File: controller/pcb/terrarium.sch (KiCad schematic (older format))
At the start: 65 parts, among them K1 G3MB-202P, K2 G3MB-202P, K3 G3MB-202P, Q1 S8050, Q2 S8050, Q3 S8050, SW1 RST, U1 ESP32-WROOM-32, U2 DS3231M, U5 TCA9548APWR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

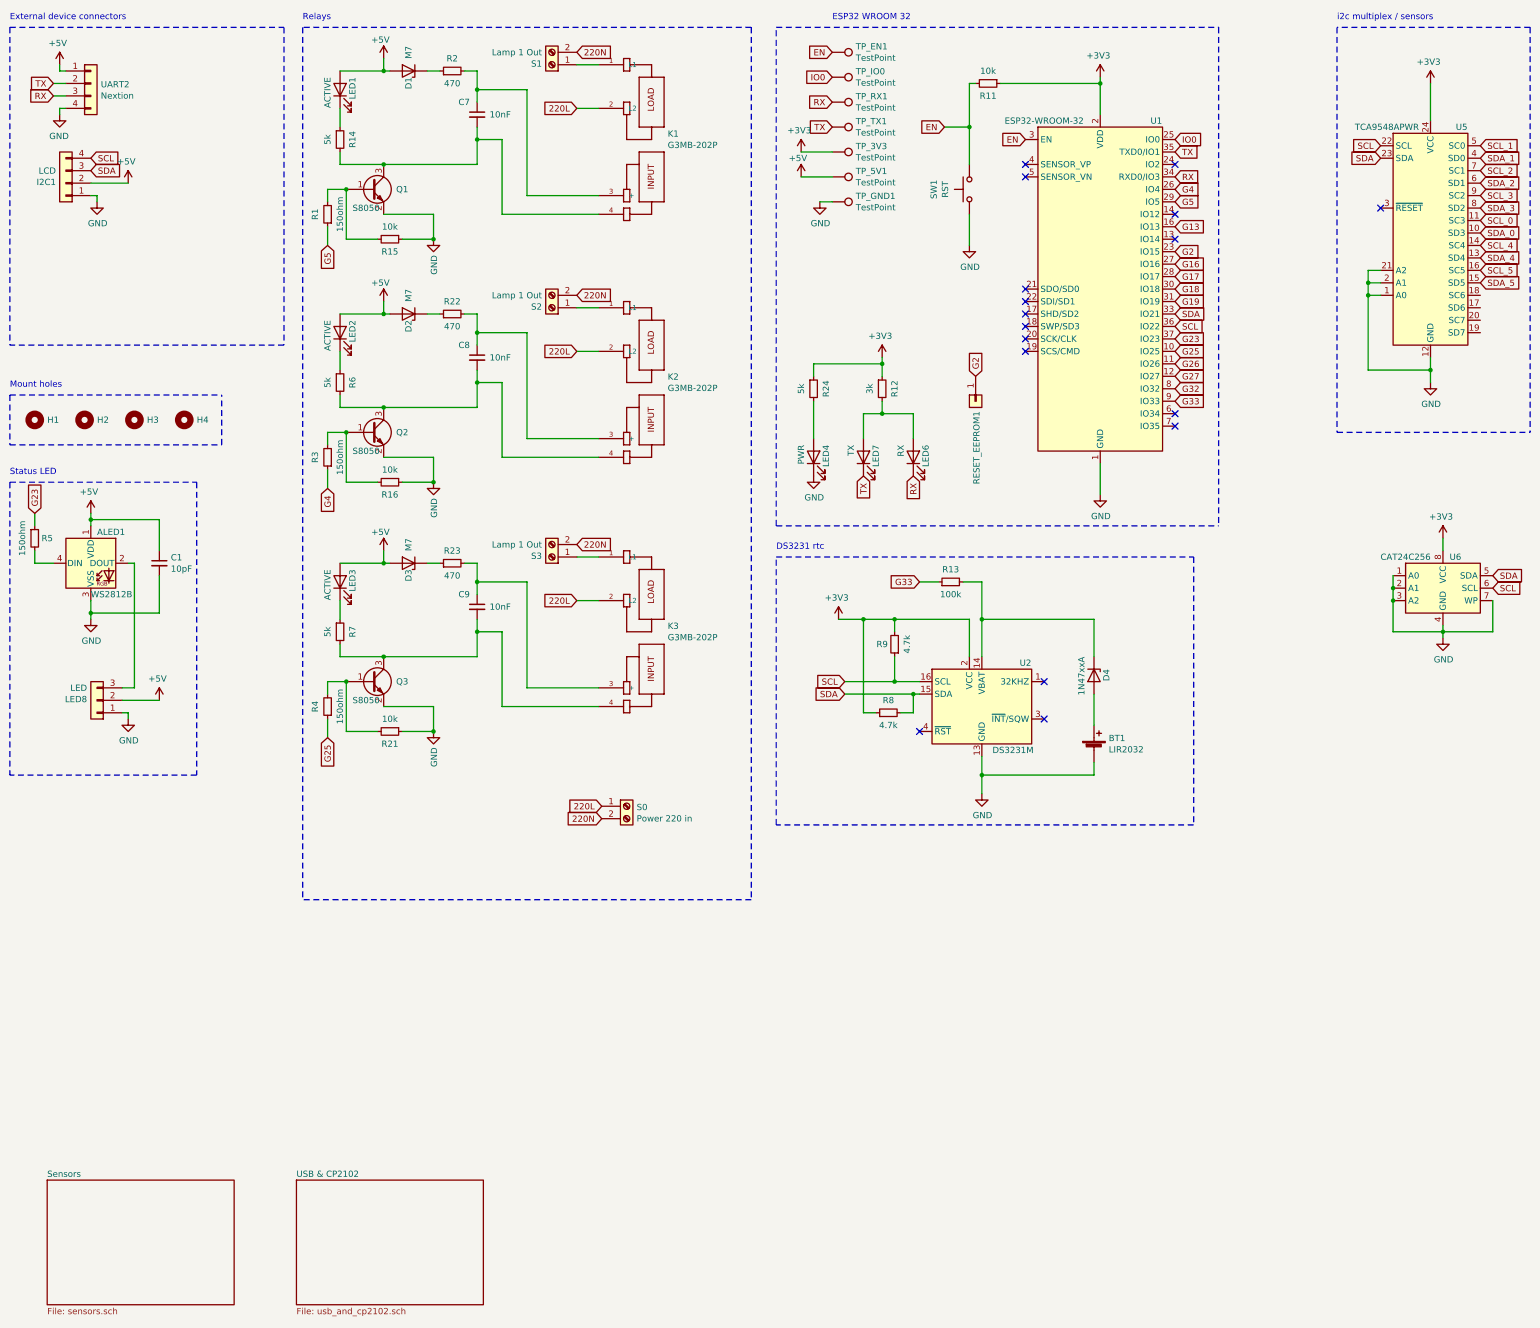
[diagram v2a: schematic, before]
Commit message: improved silk screen, tracing
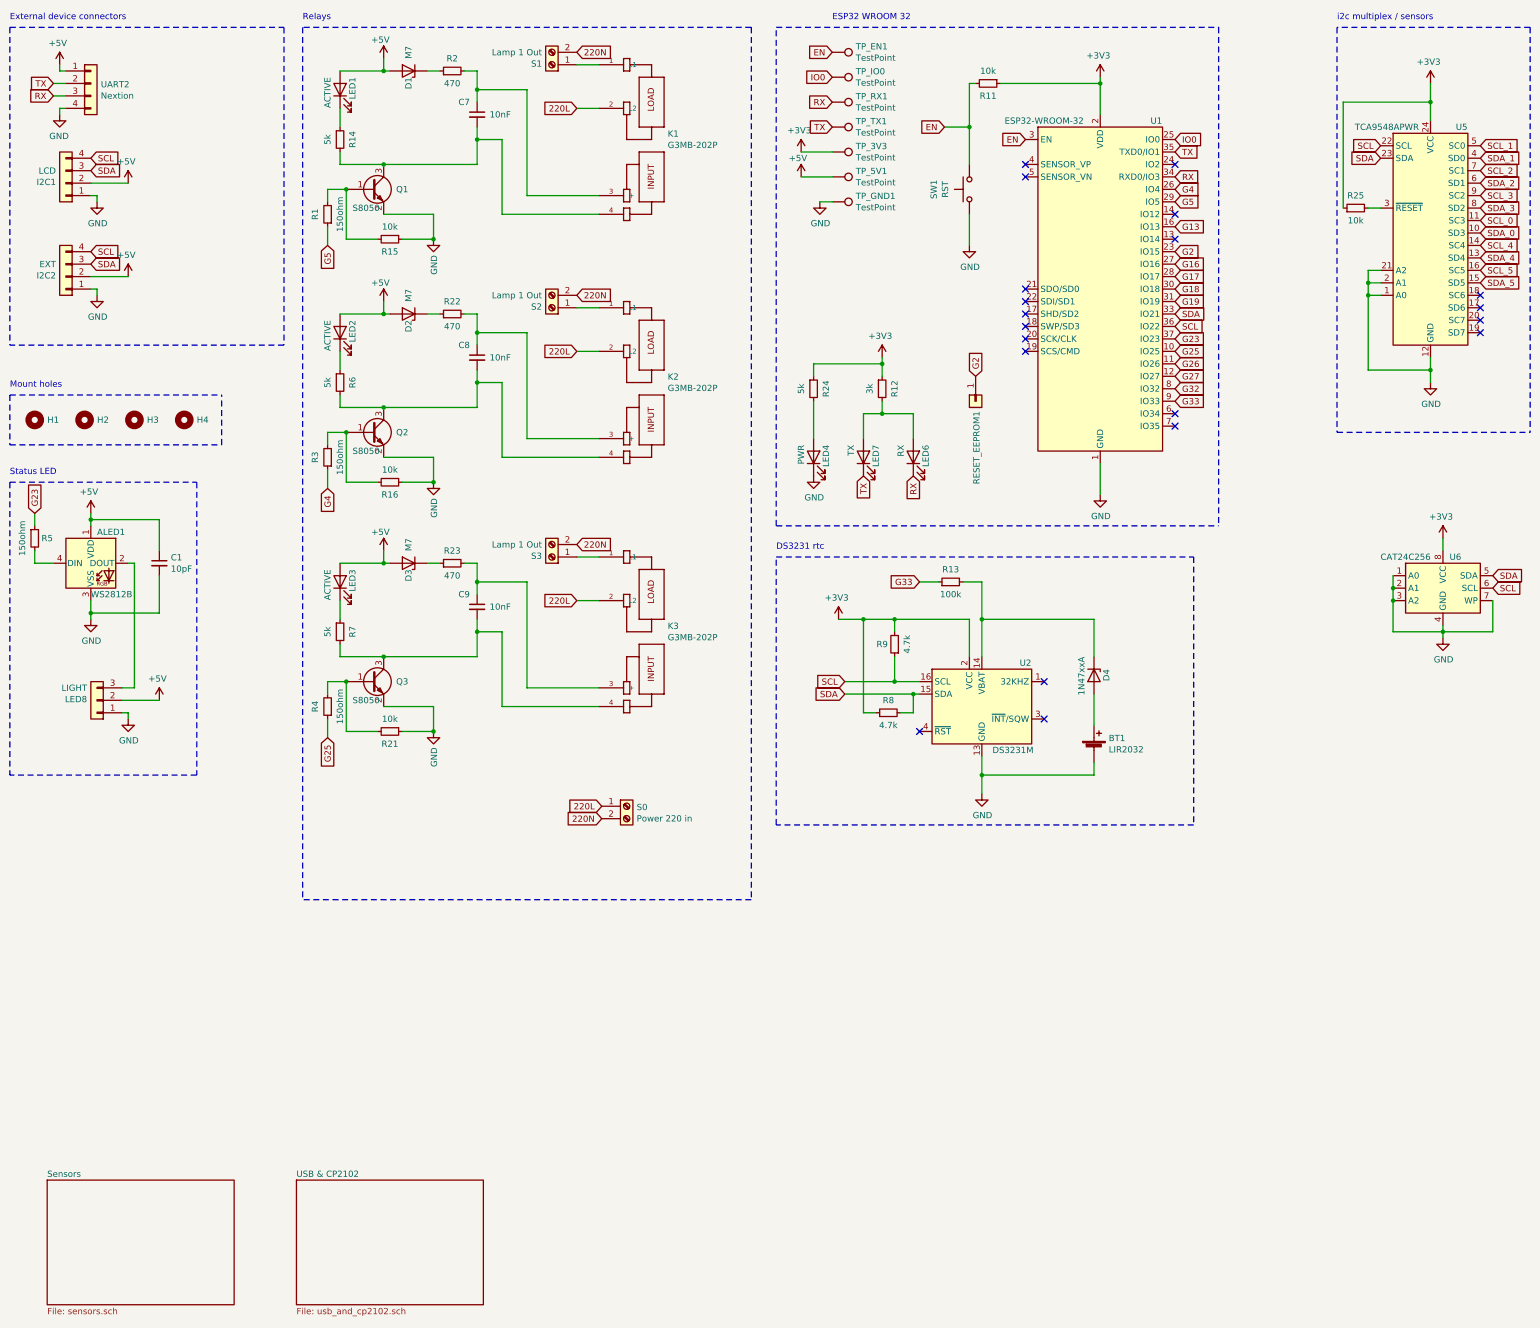
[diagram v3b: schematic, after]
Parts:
- added I2C2: EXT, Connector_JST:JST_XH_B4B-XH-A_1x04_P2.50mm_Vertical, symbol Connector_Generic:Conn_01x04
- added R25: 10k, Resistor_SMD:R_1206_3216Metric, symbol Device:R_Small
- I2C1, UART2: footprint Connector_JST:JST_XH_B4B-XH-AM_1x04_P2.50mm_Vertical -> Connector_JST:JST_XH_B4B-XH-A_1x04_P2.50mm_Vertical
- LED8: value LED -> LIGHT
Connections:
- net +3V3: now also R25.1
- net +5V: now also I2C2.2 (Pin_2)
- net GND: now also I2C2.1 (Pin_1)
- net SCL: now also I2C2.4 (Pin_4)
- net SDA: now also I2C2.3 (Pin_3)
- net at U5.3 (~RESET): now also R25.2
- no-connect marks 17 -> 20
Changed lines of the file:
@@
 F 0 "UART2" H 1430 1142 50  0000 L CNN
 F 1 "Nextion" H 1430 1051 50  0000 L CNN
-F 2 "Connector_JST:JST_XH_B4B-XH-AM_1x04_P2.50mm_Vertical" H 1350 1150 50  0001 C CNN
+F 2 "Connector_JST:JST_XH_B4B-XH-A_1x04_P2.50mm_Vertical" H 1350 1150 50  0001 C CNN
 F 3 "~" H 1350 1150 50  0001 C CNN
 	1    1350 1150
@@
 F 0 "I2C1" H 1230 1942 50  0000 L CNN
 F 1 "LCD" H 1230 1851 50  0000 L CNN
-F 2 "Connector_JST:JST_XH_B4B-XH-AM_1x04_P2.50mm_Vertical" H 1150 1950 50  0001 C CNN
+F 2 "Connector_JST:JST_XH_B4B-XH-A_1x04_P2.50mm_Vertical" H 1150 1950 50  0001 C CNN
 F 3 "~" H 1150 1950 50  0001 C CNN
 	1    1150 1950
@@
 Wire Wire Line
 	11600 2850 11600 2750
-NoConn ~ 11700 2150
 $Comp
 L power:+3V3 #PWR028
@@
 $EndComp
 Wire Wire Line
-	12100 1150 12100 1450
+	12100 1150 12100 1300
 Text GLabel 12500 2250 2    50   Input ~ 0
 SCL_0
@@
 P 1400 6100
 F 0 "LED8" H 1480 6092 50  0000 L CNN
-F 1 "LED" H 1480 6001 50  0000 L CNN
+F 1 "LIGHT" H 1480 6001 50  0000 L CNN
 F 2 "Connector_JST:JST_XH_B3B-XH-A_1x03_P2.50mm_Vertical" H 1400 6100 50  0001 C CNN
 F 3 "~" H 1400 6100 50  0001 C CNN
@@
 Wire Wire Line
 	7050 1900 7300 1900
+NoConn ~ 12500 2850
+NoConn ~ 12500 2950
+NoConn ~ 12500 3050
+NoConn ~ 12500 3150
+$Comp
+L Device:R_Small R25
+U 1 1 62D659A0
+P 11500 2150
+F 0 "R25" V 11600 2150 50  0000 C CNN
+F 1 "10k" V 11400 2150 50  0000 C CNN
+F 2 "Resistor_SMD:R_1206_3216Metric" H 11500 2150 50  0001 C CNN
+F 3 "~" H 11500 2150 50  0001 C CNN
+	1    11500 2150
+	0    -1   -1   0
+$EndComp
+Wire Wire Line
+	11700 2150 11600 2150
+Wire Wire Line
+	11400 2150 11400 1300
+Wire Wire Line
+	11400 1300 12100 1300
+Connection ~ 12100 1300
+Wire Wire Line
+	12100 1300 12100 1450
+$Comp
+L Connector_Generic:Conn_01x04 I2C2
+U 1 1 62D5D686
+P 1150 2700
+F 0 "I2C2" H 1230 2692 50  0000 L CNN
+F 1 "EXT" H 1230 2601 50  0000 L CNN
+F 2 "Connector_JST:JST_XH_B4B-XH-A_1x04_P2.50mm_Vertical" H 1150 2700 50  0001 C CNN
+F 3 "~" H 1150 2700 50  0001 C CNN
+	1    1150 2700
+	-1   0    0    1
+$EndComp
+Text GLabel 1350 2500 2    50   Input ~ 0
+SCL
+Text GLabel 1350 2600 2    50   Input ~ 0
+SDA
+$Comp
+L power:GND #PWR022
+U 1 1 62D5D68E
+P 1400 2850
+F 0 "#PWR022" H 1400 2600 50  0001 C CNN
+F 1 "GND" H 1405 2677 50  0000 C CNN
+F 2 "" H 1400 2850 50  0001 C CNN
+F 3 "" H 1400 2850 50  0001 C CNN
+	1    1400 2850
+	1    0    0    -1
+$EndComp
+Wire Wire Line
+	1400 2850 1400 2800
+Wire Wire Line
+	1400 2800 1350 2800
+$Comp
+L power:+5V #PWR031
+U 1 1 62D5D696
+P 1650 2700
+F 0 "#PWR031" H 1650 2550 50  0001 C CNN
+F 1 "+5V" H 1665 2873 50  0000 C CNN
+F 2 "" H 1650 2700 50  0001 C CNN
+F 3 "" H 1650 2700 50  0001 C CNN
+	1    1650 2700
+	-1   0    0    -1
+$EndComp
+Wire Wire Line
+	1650 2700 1350 2700
 $EndSCHEMATC
